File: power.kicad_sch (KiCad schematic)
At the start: 40 parts, among them U10 RT9080-18GJ5, U11 RT9080-12GJ5, U4 RT8097AHGE, U5 RT8097AHGE, U6 RT9080-28GJ5

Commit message: All key features are in the schematic.
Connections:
- net +3.3V: now also C5.1, U6.1 (VIN)
- net V_USB renamed +5V
- net +5V: no longer C5.1, U6.1 (VIN)
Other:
- note added: "This was V_USB on the AMB82-Mini. Changed it to 3.3V rail"
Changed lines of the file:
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@@
 	(generator_version "9.0")
 	(paper "A4")
+	(text "This was V_USB on the AMB82-Mini.\nChanged it to 3.3V rail\n"
+		(exclude_from_sim no)
+		(at 164.084 36.068 0)
+		(effects
+			(font
+				(size 1.27 1.27)
+			)
+		)
+	)
 	(junction
 		(at 120.65 123.19)
@@
 			)
 		)
-		(property "Value" "V_USB"
+		(property "Value" "+5V"
 			(at 116.332 42.926 0)
 			(effects
@@
 	)
 	(symbol
-		(lib_id "power:+3.3V")
-		(at 162.56 43.18 0)
+		(lib_id "Device:C_Small")
+		(at 162.56 119.38 0)
 		(unit 1)
 		(exclude_from_sim no)
@@
 		(on_board yes)
 		(dnp no)
-		(property "Reference" "#PWR076"
-			(at 162.56 46.99 0)
+		(fields_autoplaced yes)
+		(property "Reference" "C7"
+			(at 165.1 118.1162 0)
 			(effects
 				(font
 					(size 1.27 1.27)
 				)
-				(hide yes)
+				(justify left)
 			)
 		)
-		(property "Value" "V_USB"
-			(at 167.132 41.656 0)
+		(property "Value" "2.2uF/10V"
+			(at 165.1 120.6562 0)
 			(effects
 				(font
 					(size 1.27 1.27)
 				)
+				(justify left)
 			)
 		)
 		(property "Footprint" ""
-			(at 162.56 43.18 0)
+			(at 162.56 119.38 0)
 			(effects
 				(font
@@
 			)
 		)
-		(property "Datasheet" ""
-			(at 162.56 43.18 0)
+		(property "Datasheet" "~"
+			(at 162.56 119.38 0)
 			(effects
 				(font
@@
 			)
 		)
-		(property "Description" "Power symbol creates a global label with name \"+3.3V\""
-			(at 162.56 43.18 0)
+		(property "Description" "Unpolarized capacitor, small symbol"
+			(at 162.56 119.38 0)
 			(effects
 				(font
@@
 		(pin "1"
 		)
+		(pin "2"
+		)
 		(instances
 			(project "mormee-board-1"
 				(path "/d2af8ba6-fbfa-439f-91d9-67827f3f2396/6e7d7bb5-6766-4f43-bc72-7d092cc246e2"
-					(reference "#PWR076")
+					(reference "C7")
 					(unit 1)
 				)
@@
 	)
 	(symbol
-		(lib_id "Device:C_Small")
-		(at 162.56 119.38 0)
+		(lib_id "power:+3.3V")
+		(at 162.56 113.03 0)
 		(unit 1)
 		(exclude_from_sim no)
@@
 		(on_board yes)
 		(dnp no)
-		(fields_autoplaced yes)
-		(property "Reference" "C7"
-			(at 165.1 118.1162 0)
+		(property "Reference" "#PWR078"
+			(at 162.56 116.84 0)
 			(effects
 				(font
 					(size 1.27 1.27)
 				)
-				(justify left)
+				(hide yes)
 			)
 		)
-		(property "Value" "2.2uF/10V"
-			(at 165.1 120.6562 0)
+		(property "Value" "+3.3V"
+			(at 166.37 112.014 0)
 			(effects
 				(font
 					(size 1.27 1.27)
 				)
-				(justify left)
 			)
 		)
 		(property "Footprint" ""
-			(at 162.56 119.38 0)
+			(at 162.56 113.03 0)
 			(effects
 				(font
@@
 			)
 		)
-		(property "Datasheet" "~"
-			(at 162.56 119.38 0)
+		(property "Datasheet" ""
+			(at 162.56 113.03 0)
 			(effects
 				(font
@@
 			)
 		)
-		(property "Description" "Unpolarized capacitor, small symbol"
-			(at 162.56 119.38 0)
+		(property "Description" "Power symbol creates a global label with name \"+3.3V\""
+			(at 162.56 113.03 0)
 			(effects
 				(font
@@
 		(pin "1"
 		)
-		(pin "2"
-		)
 		(instances
 			(project "mormee-board-1"
 				(path "/d2af8ba6-fbfa-439f-91d9-67827f3f2396/6e7d7bb5-6766-4f43-bc72-7d092cc246e2"
-					(reference "C7")
+					(reference "#PWR078")
 					(unit 1)
 				)
@@
 	)
 	(symbol
-		(lib_id "power:+3.3V")
-		(at 162.56 113.03 0)
+		(lib_id "Device:R_US")
+		(at 48.26 34.29 90)
 		(unit 1)
 		(exclude_from_sim no)
@@
 		(on_board yes)
 		(dnp no)
-		(property "Reference" "#PWR078"
-			(at 162.56 116.84 0)
+		(fields_autoplaced yes)
+		(property "Reference" "R64"
+			(at 48.26 27.94 90)
 			(effects
 				(font
 					(size 1.27 1.27)
 				)
-				(hide yes)
 			)
 		)
-		(property "Value" "+3.3V"
-			(at 166.37 112.014 0)
+		(property "Value" "100K"
+			(at 48.26 30.48 90)
 			(effects
 				(font
@@
 		)
 		(property "Footprint" ""
-			(at 162.56 113.03 0)
+			(at 48.514 33.274 90)
 			(effects
 				(font
@@
 			)
 		)
-		(property "Datasheet" ""
-			(at 162.56 113.03 0)
+		(property "Datasheet" "~"
+			(at 48.26 34.29 0)
 			(effects
 				(font
@@
 			)
 		)
-		(property "Description" "Power symbol creates a global label with name \"+3.3V\""
-			(at 162.56 113.03 0)
+		(property "Description" "Resistor, US symbol"
+			(at 48.26 34.29 0)
 			(effects
 				(font
@@
 		(pin "1"
 		)
+		(pin "2"
+		)
 		(instances
-			(project "mormee-board-1"
+			(project ""
 				(path "/d2af8ba6-fbfa-439f-91d9-67827f3f2396/6e7d7bb5-6766-4f43-bc72-7d092cc246e2"
-					(reference "#PWR078")
+					(reference "R64")
 					(unit 1)
 				)
@@
 	)
 	(symbol
-		(lib_id "Device:R_US")
-		(at 48.26 34.29 90)
+		(lib_id "power:+3.3V")
+		(at 162.56 43.18 0)
 		(unit 1)
 		(exclude_from_sim no)
@@
 		(on_board yes)
 		(dnp no)
-		(fields_autoplaced yes)
-		(property "Reference" "R64"
-			(at 48.26 27.94 90)
+		(property "Reference" "#PWR076"
+			(at 162.56 46.99 0)
 			(effects
 				(font
 					(size 1.27 1.27)
 				)
+				(hide yes)
 			)
 		)
-		(property "Value" "100K"
-			(at 48.26 30.48 90)
+		(property "Value" "+3.3V"
+			(at 166.37 42.164 0)
 			(effects
 				(font
@@
 		)
 		(property "Footprint" ""
-			(at 48.514 33.274 90)
+			(at 162.56 43.18 0)
 			(effects
 				(font
@@
 			)
 		)
-		(property "Datasheet" "~"
-			(at 48.26 34.29 0)
+		(property "Datasheet" ""
+			(at 162.56 43.18 0)
 			(effects
 				(font
@@
 			)
 		)
-		(property "Description" "Resistor, US symbol"
-			(at 48.26 34.29 0)
+		(property "Description" "Power symbol creates a global label with name \"+3.3V\""
+			(at 162.56 43.18 0)
 			(effects
 				(font
@@
 		(pin "1"
 		)
-		(pin "2"
-		)
 		(instances
-			(project ""
+			(project "mormee-board-1"
 				(path "/d2af8ba6-fbfa-439f-91d9-67827f3f2396/6e7d7bb5-6766-4f43-bc72-7d092cc246e2"
-					(reference "R64")
+					(reference "#PWR076")
 					(unit 1)
 				)
@@
 			)
 		)
-		(property "Value" "V_USB"
+		(property "Value" "+5V"
 			(at 37.592 30.734 0)
 			(effects
@@
 			)
 		)
-		(property "Value" "V_USB"
+		(property "Value" "+5V"
 			(at 117.602 102.616 0)
 			(effects

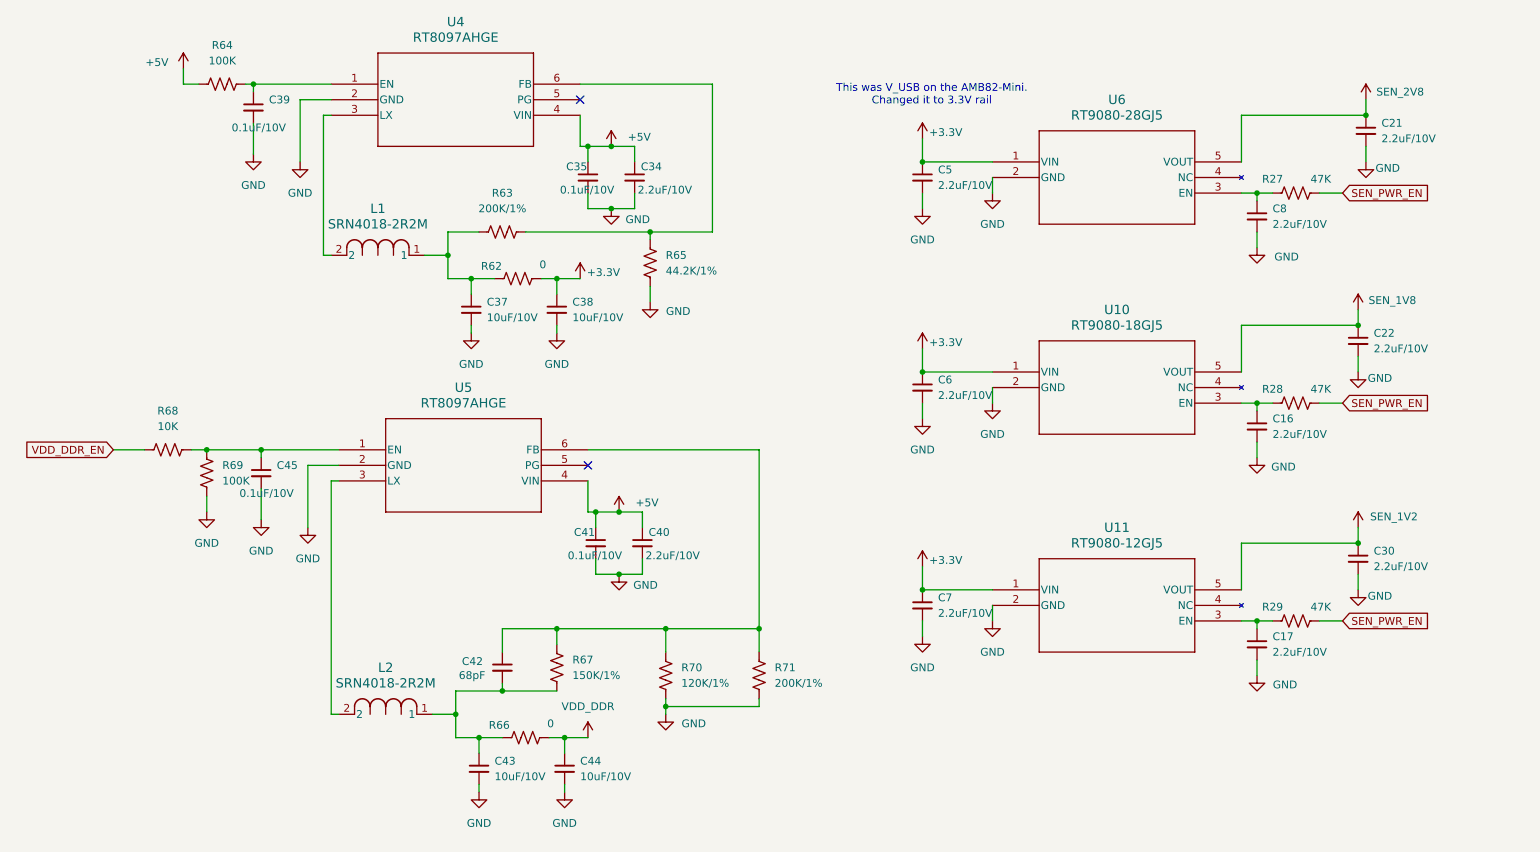
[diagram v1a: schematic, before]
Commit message: All footprints configured correctly. Next step is layout
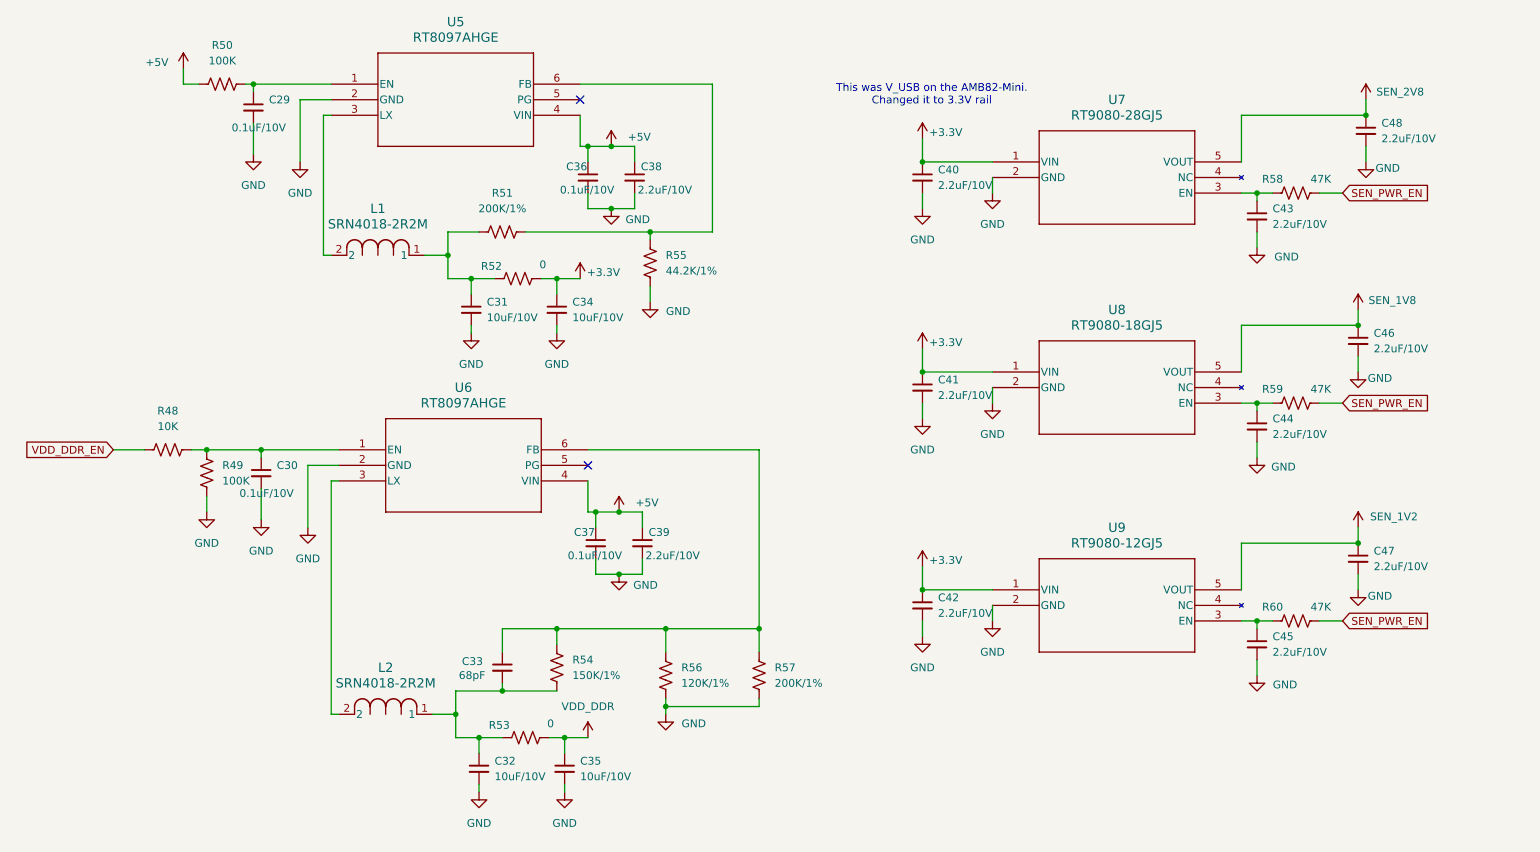
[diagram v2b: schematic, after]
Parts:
- C29: renamed from C39; footprint (none) -> Capacitor_SMD:C_0201_0603Metric_Pad0.64x0.40mm_HandSolder
- C30: renamed from C45; footprint (none) -> Capacitor_SMD:C_0201_0603Metric_Pad0.64x0.40mm_HandSolder
- C31: renamed from C37; footprint (none) -> Capacitor_SMD:C_0201_0603Metric_Pad0.64x0.40mm_HandSolder
- C32: renamed from C43; footprint (none) -> Capacitor_SMD:C_0201_0603Metric_Pad0.64x0.40mm_HandSolder
- C33: renamed from C42; footprint (none) -> Capacitor_SMD:C_0201_0603Metric_Pad0.64x0.40mm_HandSolder
- C34: renamed from C38; footprint (none) -> Capacitor_SMD:C_0201_0603Metric_Pad0.64x0.40mm_HandSolder
- C35: renamed from C44; footprint (none) -> Capacitor_SMD:C_0201_0603Metric_Pad0.64x0.40mm_HandSolder
- C36: renamed from C35; footprint (none) -> Capacitor_SMD:C_0201_0603Metric_Pad0.64x0.40mm_HandSolder
- C37: renamed from C41; footprint (none) -> Capacitor_SMD:C_0201_0603Metric_Pad0.64x0.40mm_HandSolder
- C38: renamed from C34; footprint (none) -> Capacitor_SMD:C_0201_0603Metric_Pad0.64x0.40mm_HandSolder
- C39: renamed from C40; footprint (none) -> Capacitor_SMD:C_0201_0603Metric_Pad0.64x0.40mm_HandSolder
- C40: renamed from C5; footprint (none) -> Capacitor_SMD:C_0201_0603Metric_Pad0.64x0.40mm_HandSolder
- C41: renamed from C6; footprint (none) -> Capacitor_SMD:C_0201_0603Metric_Pad0.64x0.40mm_HandSolder
- C42: renamed from C7; footprint (none) -> Capacitor_SMD:C_0201_0603Metric_Pad0.64x0.40mm_HandSolder
- C43: renamed from C8; footprint (none) -> Capacitor_SMD:C_0201_0603Metric_Pad0.64x0.40mm_HandSolder
- C44: renamed from C16; footprint (none) -> Capacitor_SMD:C_0201_0603Metric_Pad0.64x0.40mm_HandSolder
- C45: renamed from C17; footprint (none) -> Capacitor_SMD:C_0201_0603Metric_Pad0.64x0.40mm_HandSolder
- C46: renamed from C22; footprint (none) -> Capacitor_SMD:C_0201_0603Metric_Pad0.64x0.40mm_HandSolder
- C47: renamed from C30; footprint (none) -> Capacitor_SMD:C_0201_0603Metric_Pad0.64x0.40mm_HandSolder
- C48: renamed from C21; footprint (none) -> Capacitor_SMD:C_0201_0603Metric_Pad0.64x0.40mm_HandSolder
- R48: renamed from R68; footprint (none) -> Resistor_SMD:R_0201_0603Metric_Pad0.64x0.40mm_HandSolder
- R49: renamed from R69; footprint (none) -> Resistor_SMD:R_0201_0603Metric_Pad0.64x0.40mm_HandSolder
- R50: renamed from R64; footprint (none) -> Resistor_SMD:R_0201_0603Metric_Pad0.64x0.40mm_HandSolder
- R51: renamed from R63; footprint (none) -> Resistor_SMD:R_0201_0603Metric_Pad0.64x0.40mm_HandSolder
- R52: renamed from R62; footprint (none) -> Resistor_SMD:R_0201_0603Metric_Pad0.64x0.40mm_HandSolder
- R53: renamed from R66; footprint (none) -> Resistor_SMD:R_0201_0603Metric_Pad0.64x0.40mm_HandSolder
- R54: renamed from R67; footprint (none) -> Resistor_SMD:R_0201_0603Metric_Pad0.64x0.40mm_HandSolder
- R55: renamed from R65; footprint (none) -> Resistor_SMD:R_0201_0603Metric_Pad0.64x0.40mm_HandSolder
- R56: renamed from R70; footprint (none) -> Resistor_SMD:R_0201_0603Metric_Pad0.64x0.40mm_HandSolder
- R57: renamed from R71; footprint (none) -> Resistor_SMD:R_0201_0603Metric_Pad0.64x0.40mm_HandSolder
- R58: renamed from R27; footprint (none) -> Resistor_SMD:R_0201_0603Metric_Pad0.64x0.40mm_HandSolder
- R59: renamed from R28; footprint (none) -> Resistor_SMD:R_0201_0603Metric_Pad0.64x0.40mm_HandSolder
- R60: renamed from R29; footprint (none) -> Resistor_SMD:R_0201_0603Metric_Pad0.64x0.40mm_HandSolder
- U5: renamed from U4; footprint SOT-23-6_RIT -> Package_TO_SOT_SMD:SOT-23-6_Handsoldering
- U6: renamed from U5; footprint SOT-23-6_RIT -> Package_TO_SOT_SMD:SOT-23-6_Handsoldering
- renumbered U6 to U7, U10 to U8, U11 to U9

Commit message: In the middle of layout. WIP
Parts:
- added TP1: +3.3V_TP, TestPoint:TestPoint_Pad_D1.5mm, symbol Connector:TestPoint
- added TP2: +2.8V_TP, TestPoint:TestPoint_Pad_D1.5mm, symbol Connector:TestPoint
- added TP3: +1.8V_TP, TestPoint:TestPoint_Pad_D1.5mm, symbol Connector:TestPoint
- added TP4: VDD_DDR_TP, TestPoint:TestPoint_Pad_D1.5mm, symbol Connector:TestPoint
- added TP5: +1.2V_TP, TestPoint:TestPoint_Pad_D1.5mm, symbol Connector:TestPoint
- added TP9: GND_TP, TestPoint:TestPoint_Pad_D1.5mm, symbol Connector:TestPoint
- C29, C30, C36, C37: value 0.1uF/10V -> 0.1uF
- C31, C32, C34, C35: value 10uF/10V -> 10uF
- C38, C39, C40, C41, C42, C43, C44, C45, C46, C47, C48: value 2.2uF/10V -> 2.2uF
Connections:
- net +3.3V: now also TP1.1
- net GND: now also TP9.1
- net SEN_1V2: now also TP5.1
- net SEN_1V8: now also TP3.1
- net SEN_2V8: now also TP2.1
- net VDD_DDR: now also TP4.1

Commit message: Breakthrough in PCB layout. WIP
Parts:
- removed C34, C35: 10uF, Capacitor_SMD:C_0201_0603Metric_Pad0.64x0.40mm_HandSolder, symbol Device:C_Small
- removed R52, R53: 0, Resistor_SMD:R_0201_0603Metric_Pad0.64x0.40mm_HandSolder, symbol Device:R_US
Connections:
- net +3.3V: now also C31.1, L1.1, R51.1
- net VDD_DDR: now also C32.1, C33.2, L2.1, R54.1
- net L1: now reaches L1.2, U5.3 (LX)
- net L2: now reaches L2.2, U6.3 (LX)
